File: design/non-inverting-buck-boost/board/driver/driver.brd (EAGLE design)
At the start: 54.3 x 44.4 mm, 11 parts, among them IC1 L7812, IC2 78L05, T1 BC547

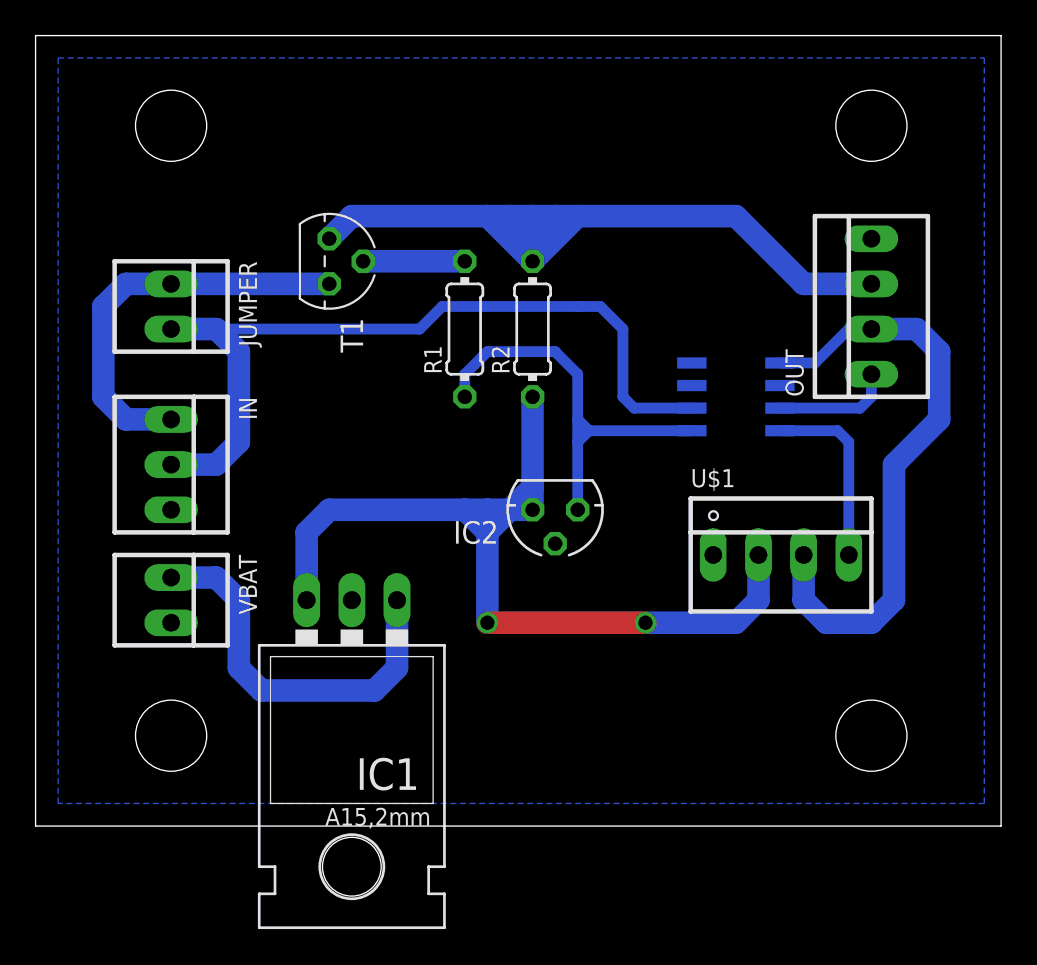
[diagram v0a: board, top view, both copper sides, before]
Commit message: new driver design with 2 ADUM3220
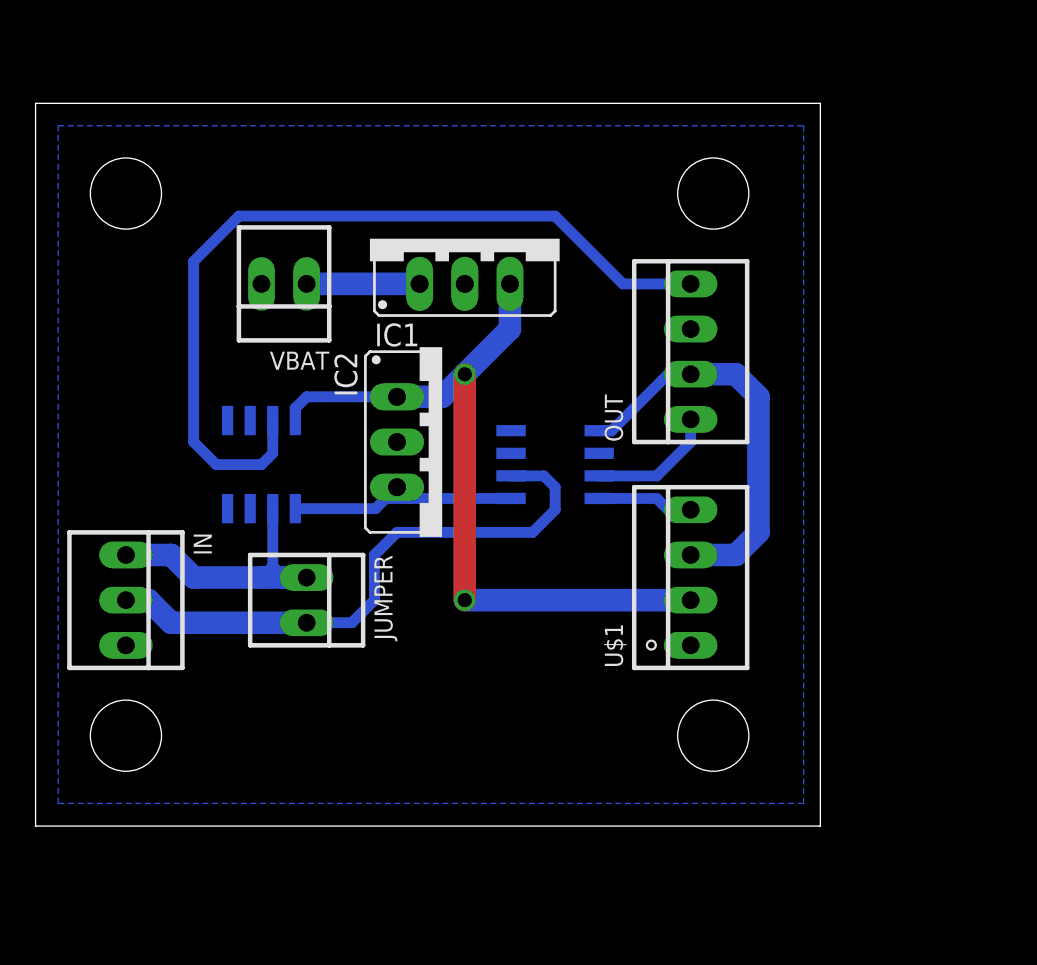
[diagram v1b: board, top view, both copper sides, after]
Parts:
- removed R1, R2: (no value), resistor:0204/7
- removed T1: BC547, transistor:TO92
- added U$3: ADUM3220, felippe:SO8
- IC1: value L7812 -> 7812; device v-reg:78XXL -> v-reg:78XXS
- IC2: value 78L05 -> 7805; device v-reg:78LXX -> v-reg:78XXS
- moved IC1 25.0 mm to (24.1, 33.0), turned to 0 degrees
- moved VBAT 18.9 mm to (14.0, 30.5), turned to 180 degrees
- moved JUMPER 18.2 mm to (15.2, 12.7)
- moved U$2 10.9 mm to (29.2, 20.3)
- moved OUT 10.5 mm to (36.8, 26.7)
- moved IN 8.03 mm to (5.08, 12.7)
- moved IC2 7.41 mm to (22.9, 21.6), turned to 270 degrees
- moved U$1 5.24 mm to (36.8, 14.0), turned to 90 degrees
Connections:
- removed net N$1: IC1.OUT, IC2.IN, R2.1, U$1.2
- removed net N$2: IC2.OUT, R1.1, U$2.1
- removed net N$4: R1.2, T1.2
- new net 12V: IC1.OUT, IC2.IN, U$1.2, U$3.8
- new net 5V: IC2.OUT, U$2.1, U$3.1
- net GND: now also OUT.3, U$3.4, U$3.5; no longer OUT.4
- net N$7: now also U$3.2; no longer T1.1
- net VG2: now also OUT.4, U$3.7; no longer OUT.3, R2.2, T1.3
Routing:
- net N$1: track 53.4 -> 0.00 mm, vias 2 -> 0
- net 12V: track 0.00 -> 42.5 mm, vias 0 -> 2
- net N$2: track 23.9 -> 0.00 mm
- net N$5: track 21.9 -> 6.35 mm
- net 5V: track 0.00 -> 14.2 mm
- net N$6: track 45.6 -> 32.8 mm
- net VS1: track 34.0 -> 22.8 mm
- net N$7: track 22.6 -> 15.7 mm
- net N$4: track 5.71 -> 0.00 mm
- net VDD2: track 10.5 -> 5.41 mm
- net VG2: track 45.9 -> 47.8 mm
- net VG1: track 6.68 -> 7.20 mm
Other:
- board size 54.3 x 44.4 mm -> 44.1 x 40.6 mm

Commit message: changed non-isolated driver to TC4422
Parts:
- removed U$3: ADUM3220, felippe:SO8
- added IC3: TC4422, felippe:DIL08
- moved VBAT 1.27 mm to (14.0, 31.8)
- moved IC1 1.27 mm to (24.1, 34.3)
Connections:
- net 12V: now also IC3.1, IC3.8; no longer U$3.8
- net 5V: no longer U$3.1
- net GND: now also IC3.4, IC3.5; no longer U$3.4, U$3.5
- net N$7: now also IC3.2; no longer U$3.2
- net VG2: now also IC3.6, IC3.7; no longer U$3.7
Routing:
- net 12V: track 42.5 -> 61.1 mm
- net VG2: track 47.8 -> 39.1 mm
- net 5V: track 14.2 -> 9.65 mm
- net N$7: track 15.7 -> 14.5 mm
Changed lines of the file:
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@@
 <element name="U$1" library="felippe" package="22-23-2041" value="B1209" x="36.83" y="13.97" rot="R90"/>
 <element name="U$2" library="felippe" package="SO8" value="ADUM3220" x="29.21" y="20.32" rot="MR90"/>
-<element name="VBAT" library="con-molex" package="22-23-2021" value="22-23-2021" x="13.97" y="30.48" rot="R180">
-<attribute name="MF" value="MOLEX" x="13.97" y="30.48" size="1.778" layer="27" rot="R180" display="off"/>
-<attribute name="MPN" value="22-23-2021" x="13.97" y="30.48" size="1.778" layer="27" rot="R180" display="off"/>
-<attribute name="OC_FARNELL" value="1462926" x="13.97" y="30.48" size="1.778" layer="27" rot="R180" display="off"/>
-<attribute name="OC_NEWARK" value="25C3832" x="13.97" y="30.48" size="1.778" layer="27" rot="R180" display="off"/>
+<element name="VBAT" library="con-molex" package="22-23-2021" value="22-23-2021" x="13.97" y="31.75" rot="R180">
+<attribute name="MF" value="MOLEX" x="13.97" y="31.75" size="1.778" layer="27" rot="R180" display="off"/>
+<attribute name="MPN" value="22-23-2021" x="13.97" y="31.75" size="1.778" layer="27" rot="R180" display="off"/>
+<attribute name="OC_FARNELL" value="1462926" x="13.97" y="31.75" size="1.778" layer="27" rot="R180" display="off"/>
+<attribute name="OC_NEWARK" value="25C3832" x="13.97" y="31.75" size="1.778" layer="27" rot="R180" display="off"/>
 </element>
-<element name="U$3" library="felippe" package="SO8" value="ADUM3220" x="12.7" y="20.32" rot="MR0"/>
 <element name="IC2" library="v-reg" package="78XXS" value="7805" x="22.86" y="21.59" rot="R270"/>
-<element name="IC1" library="v-reg" package="78XXS" value="7812" x="24.13" y="33.02"/>
+<element name="IC1" library="v-reg" package="78XXS" value="7812" x="24.13" y="34.29"/>
+<element name="IC3" library="felippe" package="DIL08" value="TC4422" x="8.89" y="22.86">
+<attribute name="MF" value="INTERNATIONAL RECTIFIER(IR)" x="8.89" y="22.86" size="1.778" layer="27" display="off"/>
+<attribute name="MPN" value="IR4426PBF" x="8.89" y="22.86" size="1.778" layer="27" display="off"/>
+<attribute name="OC_FARNELL" value="1023265" x="8.89" y="22.86" size="1.778" layer="27" display="off"/>
+<attribute name="OC_NEWARK" value="19K8460" x="8.89" y="22.86" size="1.778" layer="27" display="off"/>
+</element>
 </elements>
 <signals>
 <signal name="12V">
 <contactref element="U$1" pad="2"/>
-<contactref element="U$3" pad="8"/>
 <contactref element="IC2" pad="IN"/>
 <contactref element="IC1" pad="OUT"/>
-<wire x1="20.32" y1="24.13" x2="22.86" y2="24.13" width="1.27" layer="16"/>
+<wire x1="22.86" y1="24.13" x2="20.32" y2="24.13" width="1.27" layer="16"/>
 <wire x1="22.86" y1="24.13" x2="24.13" y2="25.4" width="1.27" layer="16"/>
 <wire x1="24.13" y1="25.4" x2="26.67" y2="27.94" width="1.27" layer="16"/>
-<wire x1="26.67" y1="27.94" x2="26.67" y2="30.48" width="1.27" layer="16"/>
-<wire x1="14.605" y1="22.7965" x2="14.605" y2="23.495" width="0.6096" layer="16"/>
-<wire x1="14.605" y1="23.495" x2="15.24" y2="24.13" width="0.6096" layer="16"/>
-<wire x1="15.24" y1="24.13" x2="20.32" y2="24.13" width="0.6096" layer="16"/>
+<wire x1="26.67" y1="27.94" x2="26.67" y2="31.75" width="1.27" layer="16"/>
 <via x="24.13" y="25.4" extent="1-16" drill="0.8" shape="square"/>
 <wire x1="24.13" y1="25.4" x2="24.13" y2="12.7" width="1.27" layer="1"/>
 <via x="24.13" y="12.7" extent="1-16" drill="0.8" shape="square"/>
 <wire x1="24.13" y1="12.7" x2="36.83" y2="12.7" width="1.27" layer="16"/>
+<wire x1="20.32" y1="24.13" x2="16.51" y2="24.13" width="1.27" layer="16"/>
+<wire x1="13.97" y1="21.59" x2="16.51" y2="24.13" width="1.27" layer="16"/>
+<contactref element="IC3" pad="8"/>
+<contactref element="IC3" pad="1"/>
+<wire x1="5.08" y1="19.05" x2="5.08" y2="21.59" width="1.27" layer="16"/>
+<wire x1="5.08" y1="21.59" x2="5.08" y2="26.67" width="1.27" layer="16"/>
+<wire x1="5.08" y1="21.59" x2="13.97" y2="21.59" width="1.27" layer="16"/>
 </signal>
 <signal name="5V">
 <contactref element="U$2" pad="1"/>
-<contactref element="U$3" pad="1"/>
 <contactref element="IC2" pad="OUT"/>
-<wire x1="14.605" y1="17.8435" x2="19.1135" y2="17.8435" width="0.6096" layer="16"/>
 <wire x1="19.685" y1="18.415" x2="20.32" y2="19.05" width="0.6096" layer="16"/>
 <wire x1="26.7335" y1="18.415" x2="20.955" y2="18.415" width="0.6096" layer="16"/>
@@
 <contactref element="VBAT" pad="1"/>
 <contactref element="IC1" pad="IN"/>
-<wire x1="15.24" y1="30.48" x2="21.59" y2="30.48" width="1.27" layer="16"/>
+<wire x1="15.24" y1="31.75" x2="21.59" y2="31.75" width="1.27" layer="16"/>
 </signal>
 <signal name="GND">
@@
 <vertex x="43.18" y="1.27"/>
 </polygon>
-<contactref element="U$3" pad="4"/>
-<contactref element="U$3" pad="5"/>
 <contactref element="IC2" pad="GND"/>
 <contactref element="IC1" pad="GND"/>
 <contactref element="OUT" pad="3"/>
+<contactref element="IC3" pad="4"/>
+<contactref element="IC3" pad="5"/>
+<wire x1="12.7" y1="26.67" x2="12.7" y2="19.05" width="0" layer="19" extent="1-1"/>
 </signal>
 <signal name="N$6">
@@
 </signal>
 <signal name="N$7">
-<contactref element="U$3" pad="2"/>
 <contactref element="JUMPER" pad="1"/>
 <contactref element="IN" pad="1"/>
-<wire x1="12.7" y1="13.97" x2="13.97" y2="13.97" width="1.27" layer="16"/>
-<wire x1="13.97" y1="13.97" x2="15.24" y2="13.97" width="1.27" layer="16"/>
-<wire x1="13.335" y1="14.605" x2="12.7" y2="13.97" width="0.6096" layer="16"/>
-<wire x1="13.335" y1="17.8435" x2="13.335" y2="14.605" width="0.6096" layer="16"/>
-<wire x1="13.335" y1="14.605" x2="13.97" y2="13.97" width="0.6096" layer="16"/>
-<wire x1="5.08" y1="15.24" x2="7.62" y2="15.24" width="1.27" layer="16"/>
+<contactref element="IC3" pad="2"/>
+<wire x1="7.62" y1="15.24" x2="5.08" y2="15.24" width="1.27" layer="16"/>
 <wire x1="7.62" y1="15.24" x2="8.89" y2="13.97" width="1.27" layer="16"/>
-<wire x1="8.89" y1="13.97" x2="12.7" y2="13.97" width="1.27" layer="16"/>
+<wire x1="8.89" y1="13.97" x2="15.24" y2="13.97" width="1.27" layer="16"/>
+<wire x1="7.62" y1="19.05" x2="7.62" y2="15.24" width="1.27" layer="16"/>
 </signal>
 <signal name="VG2">
-<contactref element="U$3" pad="7"/>
-<wire x1="13.335" y1="22.7965" x2="13.335" y2="20.955" width="0.6096" layer="16"/>
-<wire x1="11.43" y1="34.29" x2="8.89" y2="31.75" width="0.6096" layer="16"/>
 <contactref element="OUT" pad="4"/>
-<wire x1="36.83" y1="30.48" x2="33.02" y2="30.48" width="0.6096" layer="16"/>
-<wire x1="13.335" y1="20.955" x2="12.7" y2="20.32" width="0.6096" layer="16"/>
-<wire x1="12.7" y1="20.32" x2="10.16" y2="20.32" width="0.6096" layer="16"/>
-<wire x1="10.16" y1="20.32" x2="8.89" y2="21.59" width="0.6096" layer="16"/>
-<wire x1="8.89" y1="21.59" x2="8.89" y2="31.75" width="0.6096" layer="16"/>
-<wire x1="33.02" y1="30.48" x2="29.21" y2="34.29" width="0.6096" layer="16"/>
-<wire x1="29.21" y1="34.29" x2="11.43" y2="34.29" width="0.6096" layer="16"/>
+<contactref element="IC3" pad="7"/>
+<contactref element="IC3" pad="6"/>
+<wire x1="10.16" y1="26.67" x2="8.89" y2="26.67" width="1.27" layer="16"/>
+<wire x1="7.62" y1="26.67" x2="8.89" y2="26.67" width="1.27" layer="16"/>
+<wire x1="8.89" y1="26.67" x2="8.89" y2="31.75" width="1.27" layer="16"/>
+<wire x1="8.89" y1="31.75" x2="11.43" y2="34.29" width="1.27" layer="16"/>
+<wire x1="11.43" y1="34.29" x2="34.449" y2="34.29" width="1.27" layer="16"/>
+<wire x1="34.449" y1="34.29" x2="34.449" y2="34.04770625" width="1.27" layer="16"/>
+<wire x1="34.449" y1="34.04770625" x2="36.58770625" y2="31.909" width="1.27" layer="16"/>
+<wire x1="36.58770625" y1="31.909" x2="36.671" y2="31.909" width="1.27" layer="16"/>
+<wire x1="36.671" y1="31.909" x2="36.83" y2="31.75" width="1.27" layer="16"/>
+<wire x1="36.83" y1="31.75" x2="36.83" y2="30.48" width="1.27" layer="16"/>
 </signal>
 <signal name="VG1">
